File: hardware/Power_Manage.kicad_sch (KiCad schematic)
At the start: 59 parts, among them U10 TPS62088, U4 TPS62088, U6 MAX38904C, U7 MAX38904C, U8 TPS62867, U9 TPS62088

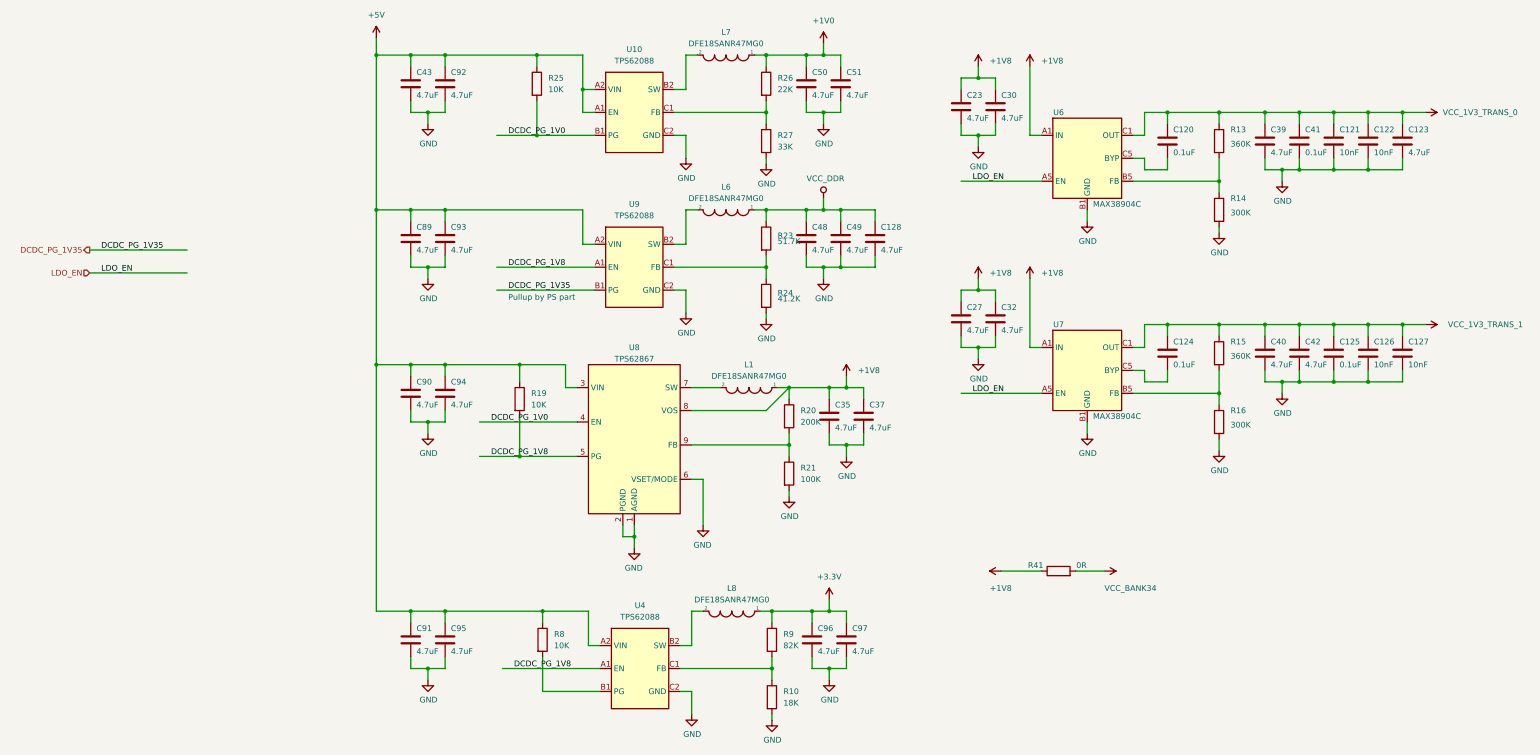
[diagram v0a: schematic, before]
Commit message: delete RF transceiver
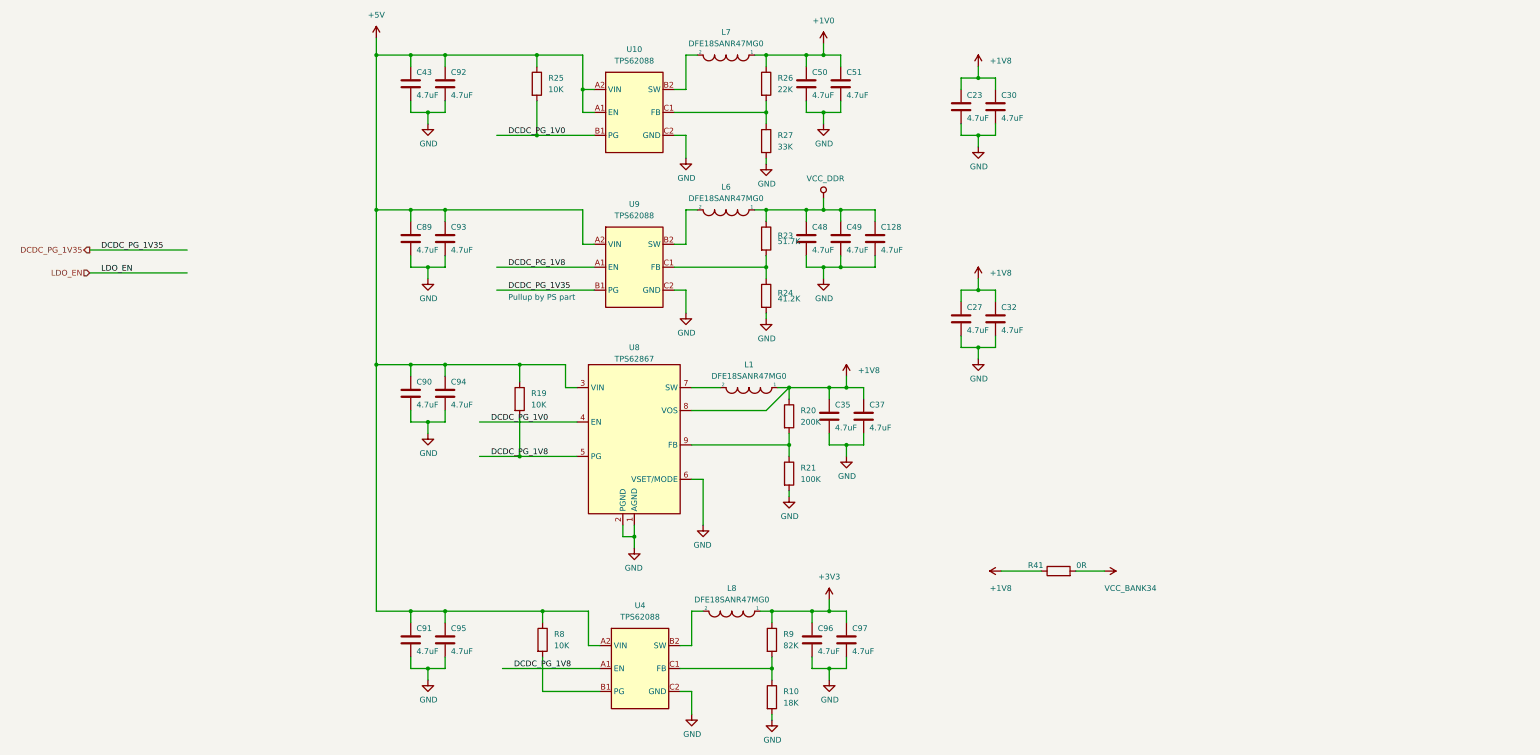
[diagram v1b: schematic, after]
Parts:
- removed C120, C124, C125, C41: 0.1uF, Capacitor_SMD:C_0402_1005Metric, symbol Device:C
- removed C121, C122, C126, C127: 10nF, Capacitor_SMD:C_0402_1005Metric, symbol Device:C
- removed C123, C39, C40, C42: 4.7uF, Capacitor_SMD:C_0402_1005Metric, symbol Device:C
- removed R13, R15: 360K, Resistor_SMD:R_0201_0603Metric, symbol Device:R
- removed R14, R16: 300K, Resistor_SMD:R_0201_0603Metric, symbol Device:R
- removed U6, U7: MAX38904C, Package_CSP_Local:wlp-15_2p168_1p338_0p5_0p4, symbol Power_Supervisor_Local:MAX38904C
